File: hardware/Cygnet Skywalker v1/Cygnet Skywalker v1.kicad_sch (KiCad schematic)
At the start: 0 parts

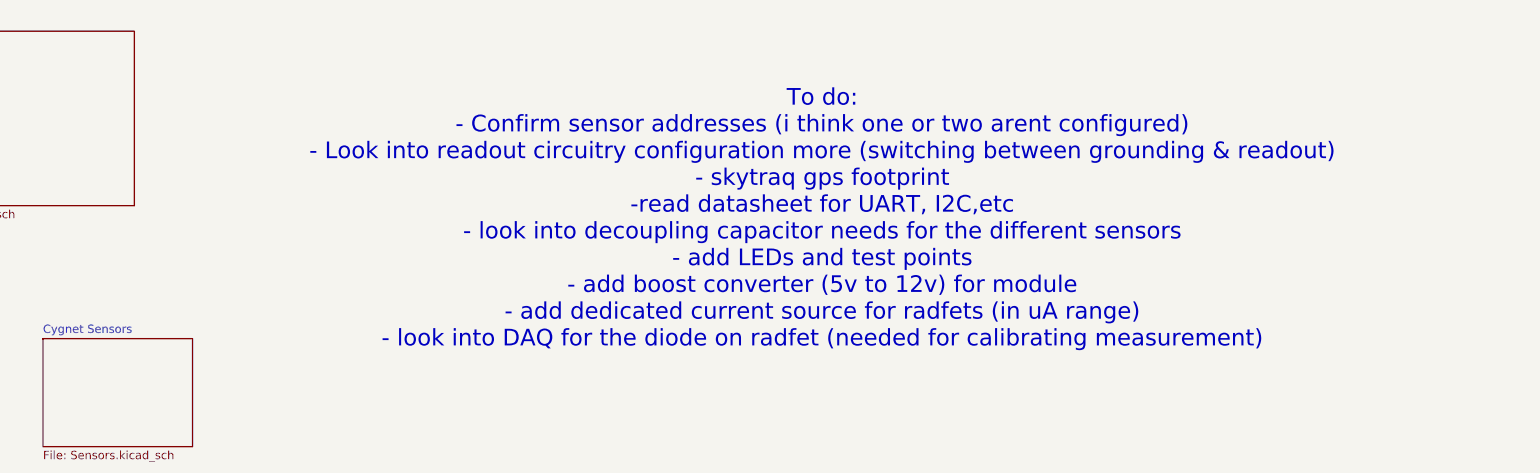
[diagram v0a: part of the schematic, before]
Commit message: minor progress on pcb design
- more decoupling caps
- i2c address config
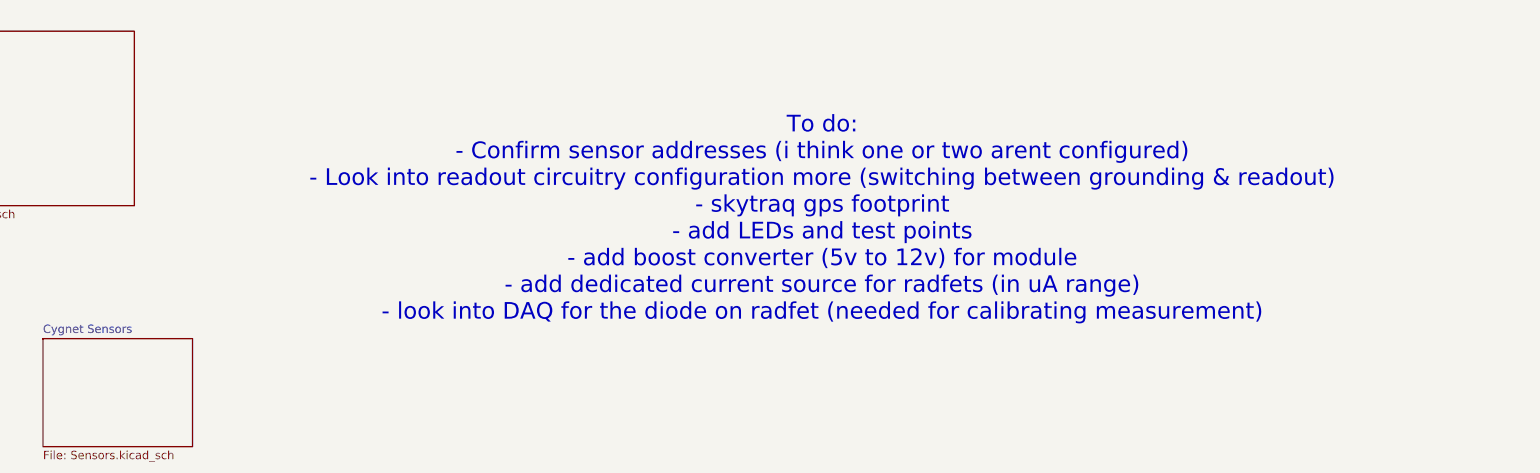
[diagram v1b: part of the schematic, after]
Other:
- note added: "To do: - Confirm sensor addresses (i think one or two arent configured) - Look into readout circuitry configuration more (switching between grounding & readout) - skytraq gps footprint - add LEDs and test points - add boost converter (5v to 12v) for module - add dedicated current source for radfets (in uA range) - look into DAQ for the diode on radfet (needed for calibrating measurement)"
- note removed: "To do: - Confirm sensor addresses (i think one or two arent configured) - Look into readout circuitry configuration more (switching between grounding & readout) - skytraq gps footprint -read datasheet for UART, I2C,etc - look into decoupling capacitor needs for the different sensors - add LEDs and test points - add boost converter (5v to 12v) for module - add dedicated current source for radfets 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"
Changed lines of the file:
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@@
 	(generator_version "9.0")
 	(paper "A4")
-	(text "To do:\n- Confirm sensor addresses (i think one or two arent configured)\n- Look into readout circuitry configuration more (switching between grounding & readout)\n- skytraq gps footprint\n-read datasheet for UART, I2C,etc \n- look into decoupling capacitor needs for the different sensors\n- add LEDs and test points\n- add boost converter (5v to 12v) for module\n- add dedicated current source for radfets (in uA range)\n- look into DAQ for the diode on radfet (needed for calibrating measurement)"
+	(text "To do:\n- Confirm sensor addresses (i think one or two arent configured)\n- Look into readout circuitry configuration more (switching between grounding & readout)\n- skytraq gps footprint\n- add LEDs and test points\n- add boost converter (5v to 12v) for module\n- add dedicated current source for radfets (in uA range)\n- look into DAQ for the diode on radfet (needed for calibrating measurement)"
 		(exclude_from_sim no)
 		(at 196.596 60.452 0)

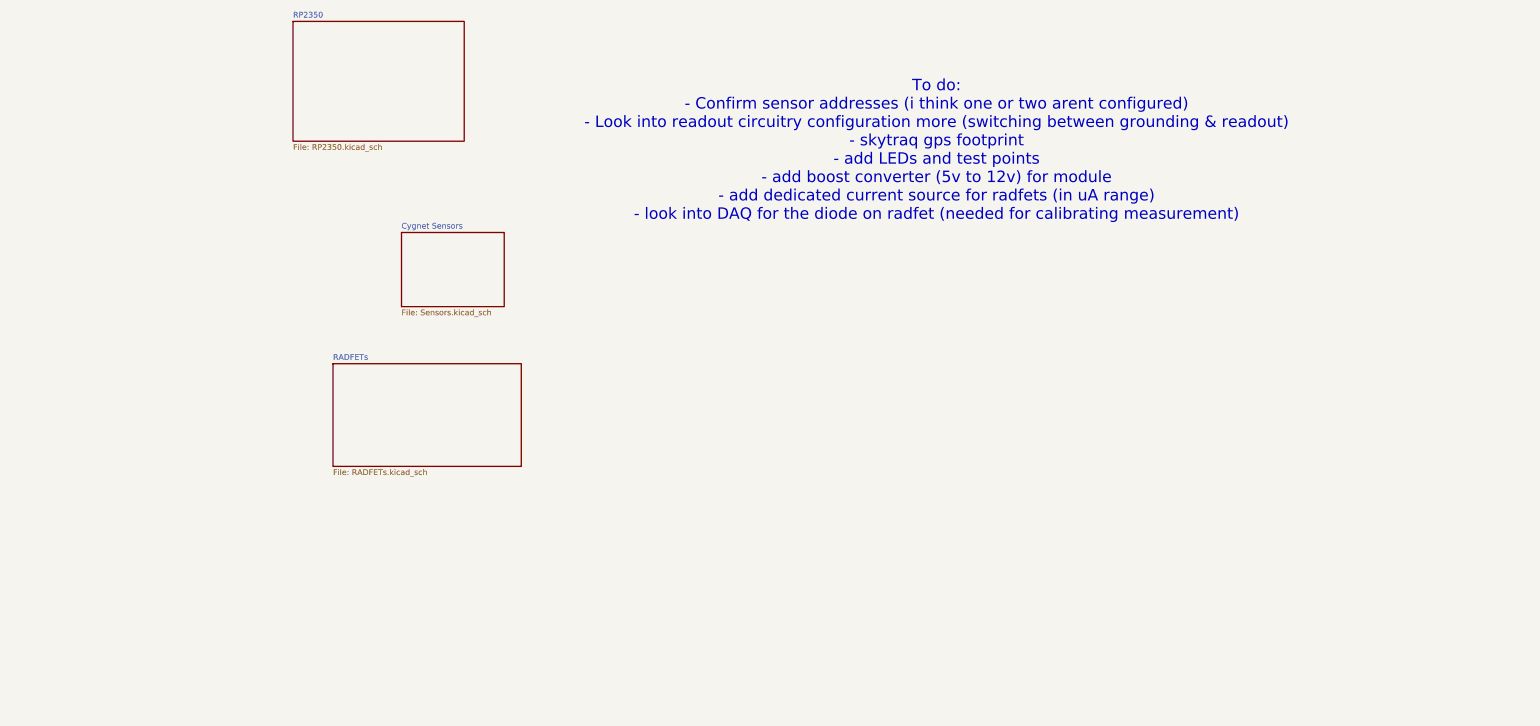
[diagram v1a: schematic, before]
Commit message: updated progress on PCB
-implemented 3.3v to 12v boost converter
-radfet readout circuitry done (i think)
-added readout circuitry from oresat & proves fc v5c board
-finished gps schematic (need footprint still)
-added few LEDs

main priorities:
-watchdog circuit
-calculate voltage div resistor values for 12v
-gps footprint
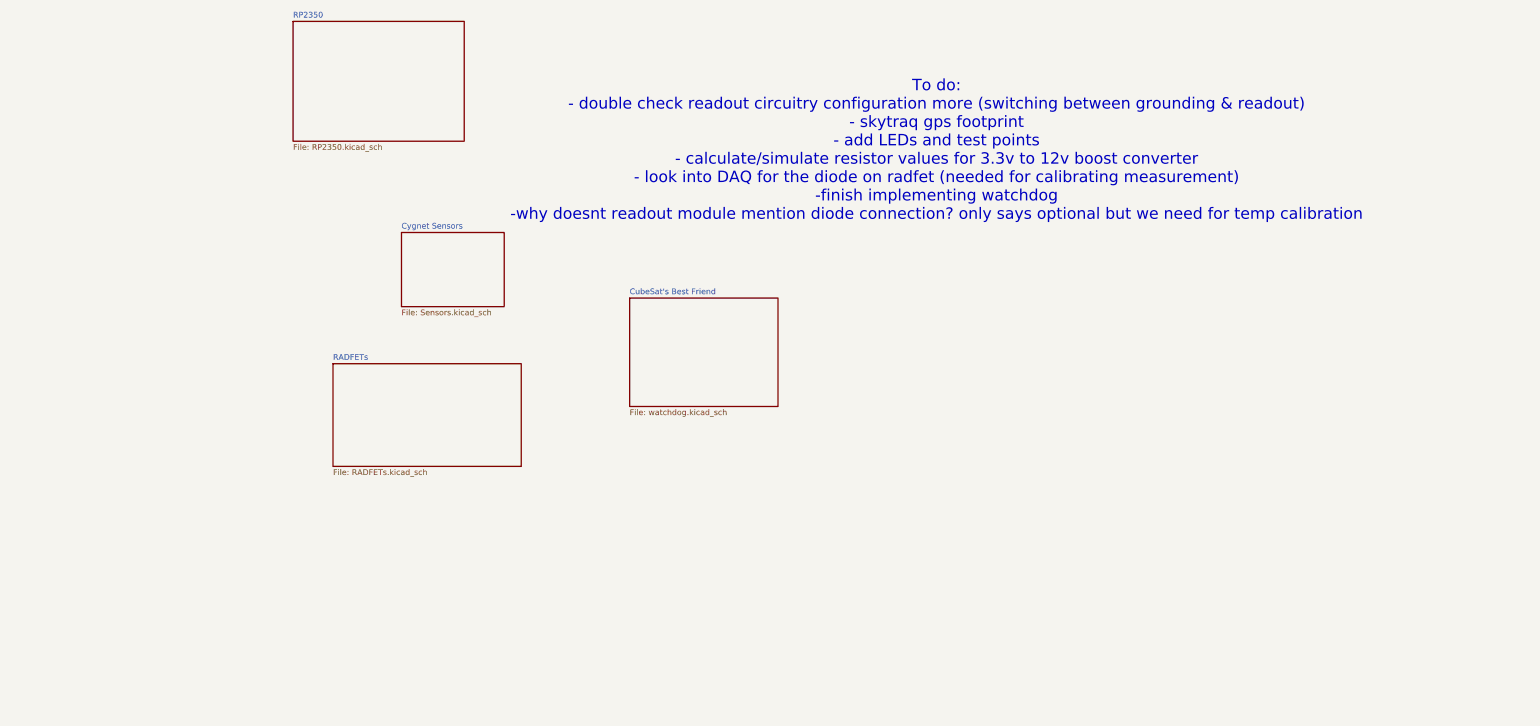
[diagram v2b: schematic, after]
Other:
- added sheet CubeSat's Best Friend (watchdog.kicad_sch)
- note added: "To do: - double check readout circuitry configuration more (switching between grounding & readout) - skytraq gps footprint - add LEDs and test points - calculate/simulate resistor values for 3.3v to 12v boost converter - look into DAQ for the diode on radfet (needed for calibrating measurement) -finish implementing watchdog -why doesnt readout module mention diode connection? only says optional b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"
- note removed: "To do: - Confirm sensor addresses (i think one or two arent configured) - Look into readout circuitry configuration more (switching between grounding & readout) - skytraq gps footprint - add LEDs and test points - add boost converter (5v to 12v) for module - add dedicated current source for radfets (in uA range) - look into DAQ for the diode on radfet (needed for calibrating measurement)"
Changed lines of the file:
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@@
 	(generator_version "9.0")
 	(paper "A4")
-	(text "To do:\n- Confirm sensor addresses (i think one or two arent configured)\n- Look into readout circuitry configuration more (switching between grounding & readout)\n- skytraq gps footprint\n- add LEDs and test points\n- add boost converter (5v to 12v) for module\n- add dedicated current source for radfets (in uA range)\n- look into DAQ for the diode on radfet (needed for calibrating measurement)"
+	(text "To do:\n- double check readout circuitry configuration more (switching between grounding & readout)\n- skytraq gps footprint\n- add LEDs and test points\n- calculate/simulate resistor values for 3.3v to 12v boost converter\n- look into DAQ for the diode on radfet (needed for calibrating measurement)\n-finish implementing watchdog\n-why doesnt readout module mention diode connection? only says optional but we need for temp calibration\n"
 		(exclude_from_sim no)
 		(at 196.596 60.452 0)
@@
 				)
 			)
+		)
+	)
+	(sheet
+		(at 128.27 93.345)
+		(size 33.02 24.13)
+		(exclude_from_sim no)
+		(in_bom yes)
+		(on_board yes)
+		(dnp no)
+		(fields_autoplaced yes)
+		(stroke
+			(width 0.1524)
+			(type solid)
+		)
+		(fill
+			(color 0 0 0 0.0000)
+		)
+		(property "Sheetname" "CubeSat's Best Friend"
+			(at 128.27 92.6334 0)
+			(effects
+				(font
+					(size 1.27 1.27)
+				)
+				(justify left bottom)
+			)
+		)
+		(property "Sheetfile" "watchdog.kicad_sch"
+			(at 128.27 118.0596 0)
+			(effects
+				(font
+					(size 1.27 1.27)
+				)
+				(justify left top)
+			)
+		)
+		(instances
+			(project "Cygnet Skywalker v1"
+				(path "/f674abc6-f811-4b69-a04b-9059ca6b6a44"
+					(page "5")
+				)
+			)

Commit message: modified notes
- will be adding nand flash for more long term storage of gps and radfet data & telemetry
- gps footprint not finished but started. will finish when i get access to a mouse
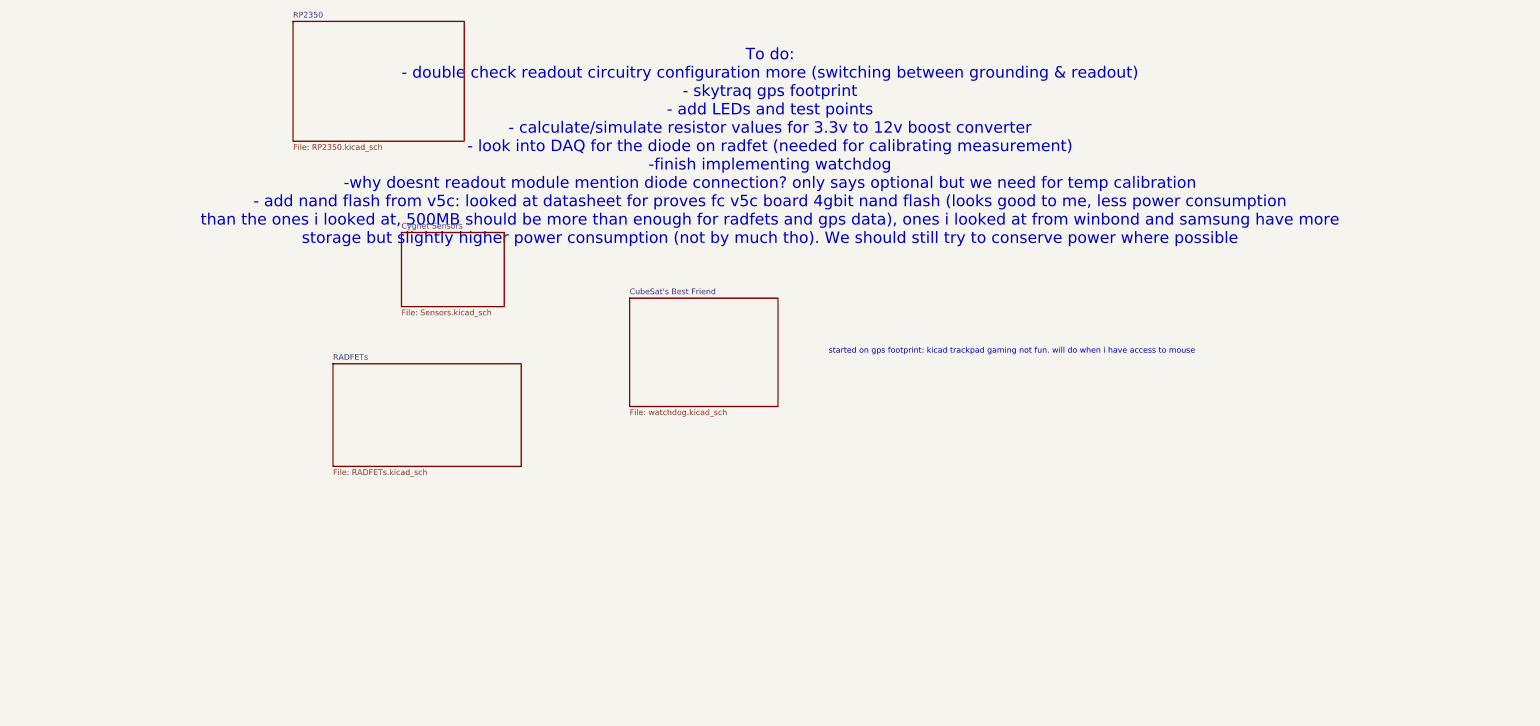
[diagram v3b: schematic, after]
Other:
- note added: "started on gps footprint: kicad trackpad gaming not fun. will do when i have access to mouse"
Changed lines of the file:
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@@
 	(generator_version "9.0")
 	(paper "A4")
-	(text "To do:\n- double check readout circuitry configuration more (switching between grounding & readout)\n- skytraq gps footprint\n- add LEDs and test points\n- calculate/simulate resistor values for 3.3v to 12v boost converter\n- look into DAQ for the diode on radfet (needed for calibrating measurement)\n-finish implementing watchdog\n-why doesnt readout module mention diode connection? only says optional but we need for temp calibration\n"
+	(text "started on gps footprint: kicad trackpad gaming not fun. will do when i have access to mouse"
 		(exclude_from_sim no)
-		(at 196.596 60.452 0)
+		(at 213.36 105.156 0)
 		(effects
 			(font
+				(size 1.27 1.27)
+			)
+		)
+	)
+	(text "To do:\n- double check readout circuitry configuration more (switching between grounding & readout)\n- skytraq gps footprint\n- add LEDs and test points\n- calculate/simulate resistor values for 3.3v to 12v boost converter\n- look into DAQ for the diode on radfet (needed for calibrating measurement)\n-finish implementing watchdog\n-why doesnt readout module mention diode connection? only says optional but we need for temp calibration\n- add nand flash from v5c: looked at datasheet for proves fc v5c board 4gbit nand flash (looks good to me, less power consumption \nthan the ones i looked at, 500MB should be more than enough for radfets and gps data), ones i looked at from winbond and samsung have more\nstorage but slightly higher power consumption (not by much tho). We should still try to conserve power where possible\n"
+		(exclude_from_sim no)
+		(at 159.512 59.69 0)
+		(effects
+			(font

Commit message: updated schematic organization & footprint edits
- refined gps footprint
- reorganized schematic
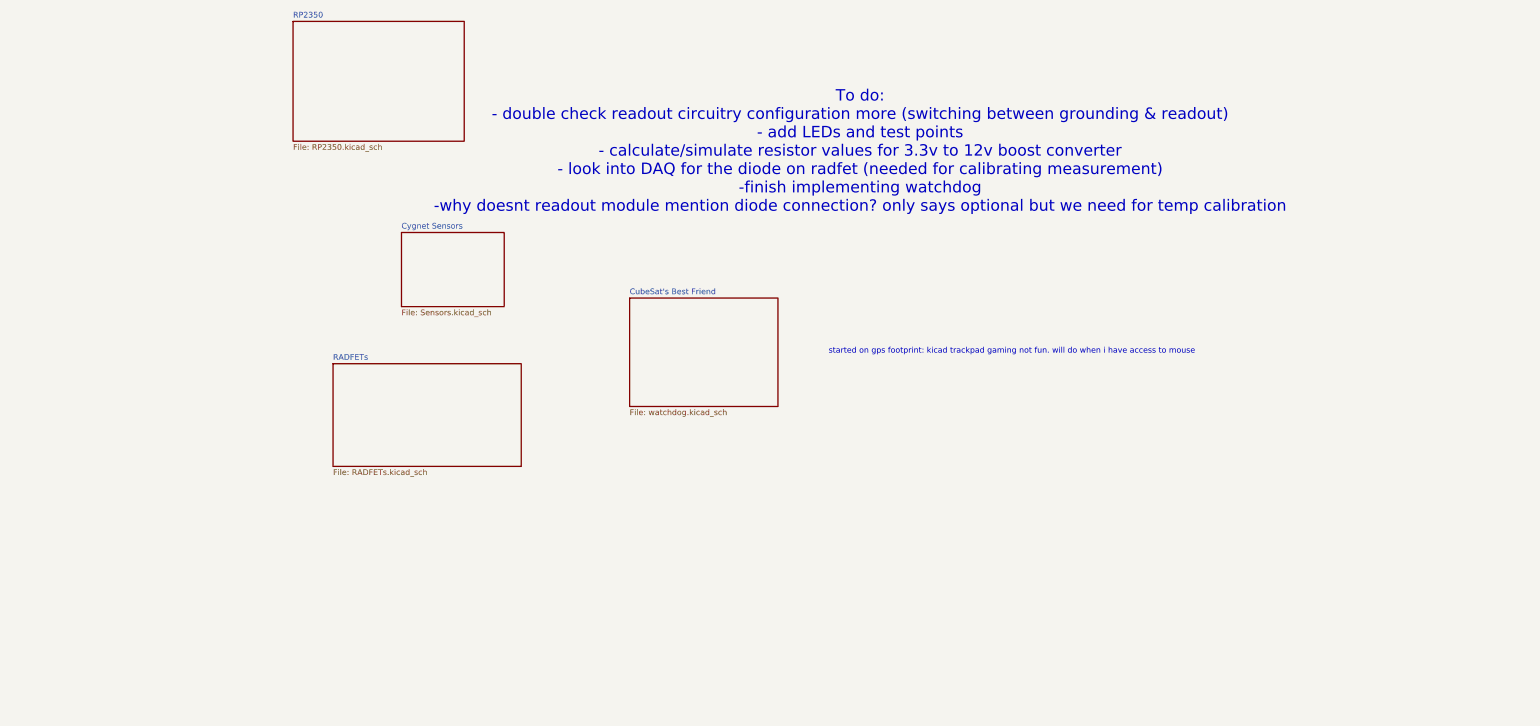
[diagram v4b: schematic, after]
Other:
- note added: "To do: - double check readout circuitry configuration more (switching between grounding & readout) - add LEDs and test points - calculate/simulate resistor values for 3.3v to 12v boost converter - look into DAQ for the diode on radfet (needed for calibrating measurement) -finish implementing watchdog -why doesnt readout module mention diode connection? only says optional but we need for temp cali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"
- note removed: "To do: - double check readout circuitry configuration more (switching between grounding & readout) - skytraq gps footprint - add LEDs and test points - calculate/simulate resistor values for 3.3v to 12v boost converter - look into DAQ for the diode on radfet (needed for calibrating measurement) -finish implementing watchdog -why doesnt readout module mention diode connection? only says optional b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"
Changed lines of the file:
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@@
 		)
 	)
-	(text "To do:\n- double check readout circuitry configuration more (switching between grounding & readout)\n- skytraq gps footprint\n- add LEDs and test points\n- calculate/simulate resistor values for 3.3v to 12v boost converter\n- look into DAQ for the diode on radfet (needed for calibrating measurement)\n-finish implementing watchdog\n-why doesnt readout module mention diode connection? only says optional but we need for temp calibration\n- add nand flash from v5c: looked at datasheet for proves fc v5c board 4gbit nand flash (looks good to me, less power consumption \nthan the ones i looked at, 500MB should be more than enough for radfets and gps data), ones i looked at from winbond and samsung have more\nstorage but slightly higher power consumption (not by much tho). We should still try to conserve power where possible\n"
+	(text "To do:\n- double check readout circuitry configuration more (switching between grounding & readout)\n- add LEDs and test points\n- calculate/simulate resistor values for 3.3v to 12v boost converter\n- look into DAQ for the diode on radfet (needed for calibrating measurement)\n-finish implementing watchdog\n-why doesnt readout module mention diode connection? only says optional but we need for temp calibration\n"
 		(exclude_from_sim no)
-		(at 159.512 59.69 0)
+		(at 179.578 60.706 0)
 		(effects
 			(font

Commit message: brought over changes made on max branch
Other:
- note added: "To do: - double check readout circuitry configuration more (switching between grounding & readout) - calculate/simulate resistor values for 3.3v to 12v boost converter -why doesnt readout module mention diode connection? only says optional but we need for temp calibration -reach out to varadis"
- note removed: "To do: - double check readout circuitry configuration more (switching between grounding & readout) - add LEDs and test points - calculate/simulate resistor values for 3.3v to 12v boost converter - look into DAQ for the diode on radfet (needed for calibrating measurement) -finish implementing watchdog -why doesnt readout module mention diode connection? only says optional but we need for temp cali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"
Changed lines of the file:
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@@
 		)
 	)
-	(text "To do:\n- double check readout circuitry configuration more (switching between grounding & readout)\n- add LEDs and test points\n- calculate/simulate resistor values for 3.3v to 12v boost converter\n- look into DAQ for the diode on radfet (needed for calibrating measurement)\n-finish implementing watchdog\n-why doesnt readout module mention diode connection? only says optional but we need for temp calibration\n"
+	(text "To do:\n- double check readout circuitry configuration more (switching between grounding & readout)\n- calculate/simulate resistor values for 3.3v to 12v boost converter\n-why doesnt readout module mention diode connection? only says optional but we need for temp calibration\n-reach out to varadis"
 		(exclude_from_sim no)
 		(at 179.578 60.706 0)
